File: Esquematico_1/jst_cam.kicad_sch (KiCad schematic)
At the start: 1 part, among them U5 AT7456E

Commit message: Update de algo nsq que puta
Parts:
- added J1, J2: Screw_Terminal_01x04, symbol Connector:Screw_Terminal_01x04
- added J3: Screw_Terminal_01x06, symbol Connector:Screw_Terminal_01x06
- added J4: Screw_Terminal_01x08, symbol Connector:Screw_Terminal_01x08
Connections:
- new net ELRS_UART_RX: J1.2 (Pin_2)
- new net ELRS_UART_TX: J1.1 (Pin_1)
- new net GND: J1.4 (Pin_4), J2.4 (Pin_4), J3.5 (Pin_5), J3.6 (Pin_6), J4.8 (Pin_8)
- new net V++: J3.4 (Pin_4)
- new net VIDEO_OSD_OUT: J3.3 (Pin_3)
- new net VTX_UART_RX: J3.2 (Pin_2)
- new net VTX_UART_TX: J3.1 (Pin_1)
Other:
- note added: "JST CAMARA"
- note added: "JST ELRS"
- note added: "JST ESC 4-1"
- note added: "JST VTX"
- moved on the sheet: U5

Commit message: Update
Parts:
- added C20: 10u, symbol Device:C
- added C21: 100n, symbol Device:C
- added FB2: FerriteBead, symbol Device:FerriteBead
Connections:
- net GND: now also C20.1, C21.1
- net MCO2: now reaches U5.5 (CLKIN)
- net 5v: now reaches J1.3 (Pin_3)
- net 5v: now also FB2.1
- new net 5vA: C20.2, C21.2, FB2.2
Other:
- moved on the sheet: J1, J2, J3, J4, U5

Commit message: Chau OSD
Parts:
- removed C20: 10u, symbol Device:C
- removed C21: 100n, symbol Device:C
- removed FB2: FerriteBead, symbol Device:FerriteBead
- removed U5: AT7456E, AT7456E:TSSOP-28_L9.7-W4.4-P0.65-LS6.4-BL-EP-2, symbol AT7456E:AT7456E
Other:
- note removed: "OSD"
- moved on the sheet: J1, J3, J4

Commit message: Correciones de tags
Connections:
- net VIDEO_OSD_OUT renamed VIDEO
- net VTX_UART_RX renamed RX_VTX
- net VTX_UART_TX renamed TX_VTX
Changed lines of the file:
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@@
 		)
 	)
-	(global_label "VTX_UART_TX"
+	(global_label "TX_VTX"
 		(shape input)
 		(at 119.38 35.56 180)
@@
 		)
 		(property "Intersheetrefs" "${INTERSHEET_REFS}"
-			(at 103.8841 35.56 0)
+			(at 109.5084 35.56 0)
 			(effects
 				(font
@@
 		)
 	)
-	(global_label "VIDEO_OSD_OUT"
+	(global_label "VIDEO"
 		(shape input)
 		(at 119.38 43.18 180)
@@
 		)
 		(property "Intersheetrefs" "${INTERSHEET_REFS}"
-			(at 101.1021 43.18 0)
+			(at 110.4759 43.18 0)
 			(effects
 				(font
@@
 		)
 	)
-	(global_label "VTX_UART_RX"
+	(global_label "RX_VTX"
 		(shape input)
 		(at 119.38 39.37 180)
@@
 		)
 		(property "Intersheetrefs" "${INTERSHEET_REFS}"
-			(at 103.5817 39.37 0)
+			(at 109.206 39.37 0)
 			(effects
 				(font
@@
 		)
 	)
-	(global_label "5v"
-		(shape input)
-		(at 186.69 48.26 180)
-		(fields_autoplaced yes)
-		(effects
-			(font
-				(size 1.27 1.27)
-				(thickness 0.254)
-				(bold yes)
-			)
-			(justify right)
-		)
-		(property "Intersheetrefs" "${INTERSHEET_REFS}"
-			(at 181.0517 48.26 0)
-			(effects
-				(font
-					(size 1.27 1.27)
-				)
-				(justify right)
-				(hide yes)
-			)
-		)
-	)
 	(symbol
 		(lib_id "power:GND")
@@
 					(unit 1)
 				)
+			)
+		)
+	)
+	(symbol
+		(lib_id "power:+3.3V")
+		(at 186.69 48.26 90)
+		(unit 1)
+		(exclude_from_sim no)
+		(in_bom yes)
+		(on_board yes)
+		(dnp no)
+		(fields_autoplaced yes)
+		(property "Reference" "#PWR027"
+			(at 190.5 48.26 0)
+			(effects
+				(font
+					(size 1.27 1.27)
+				)
+				(hide yes)
+			)
+		)
+		(property "Value" "5v"
+			(at 182.88 48.2599 90)
+			(effects
+				(font
+					(size 1.27 1.27)
+				)
+				(justify left)
+			)
+		)
+		(property "Footprint" ""
+			(at 186.69 48.26 0)
+			(effects
+				(font
+					(size 1.27 1.27)
+				)
+				(hide yes)
+			)
+		)
+		(property "Datasheet" ""
+			(at 186.69 48.26 0)
+			(effects
+				(font
+					(size 1.27 1.27)
+				)
+				(hide yes)
+			)
+		)
+		(property "Description" "Power symbol creates a global label with name \"+3.3V\""
+			(at 186.69 48.26 0)
+			(effects
+				(font
+					(size 1.27 1.27)
+				)
+				(hide yes)
+			)
+		)
+		(pin "1"
+		)
+		(instances
+			(project "Esquematico_1"
+				(path "/de2d80c1-c21c-478d-b724-17659b714c38/457e76de-adfe-4ec5-a818-c5970caa89a7"
+					(reference "#PWR027")
+					(unit 1)
+				)

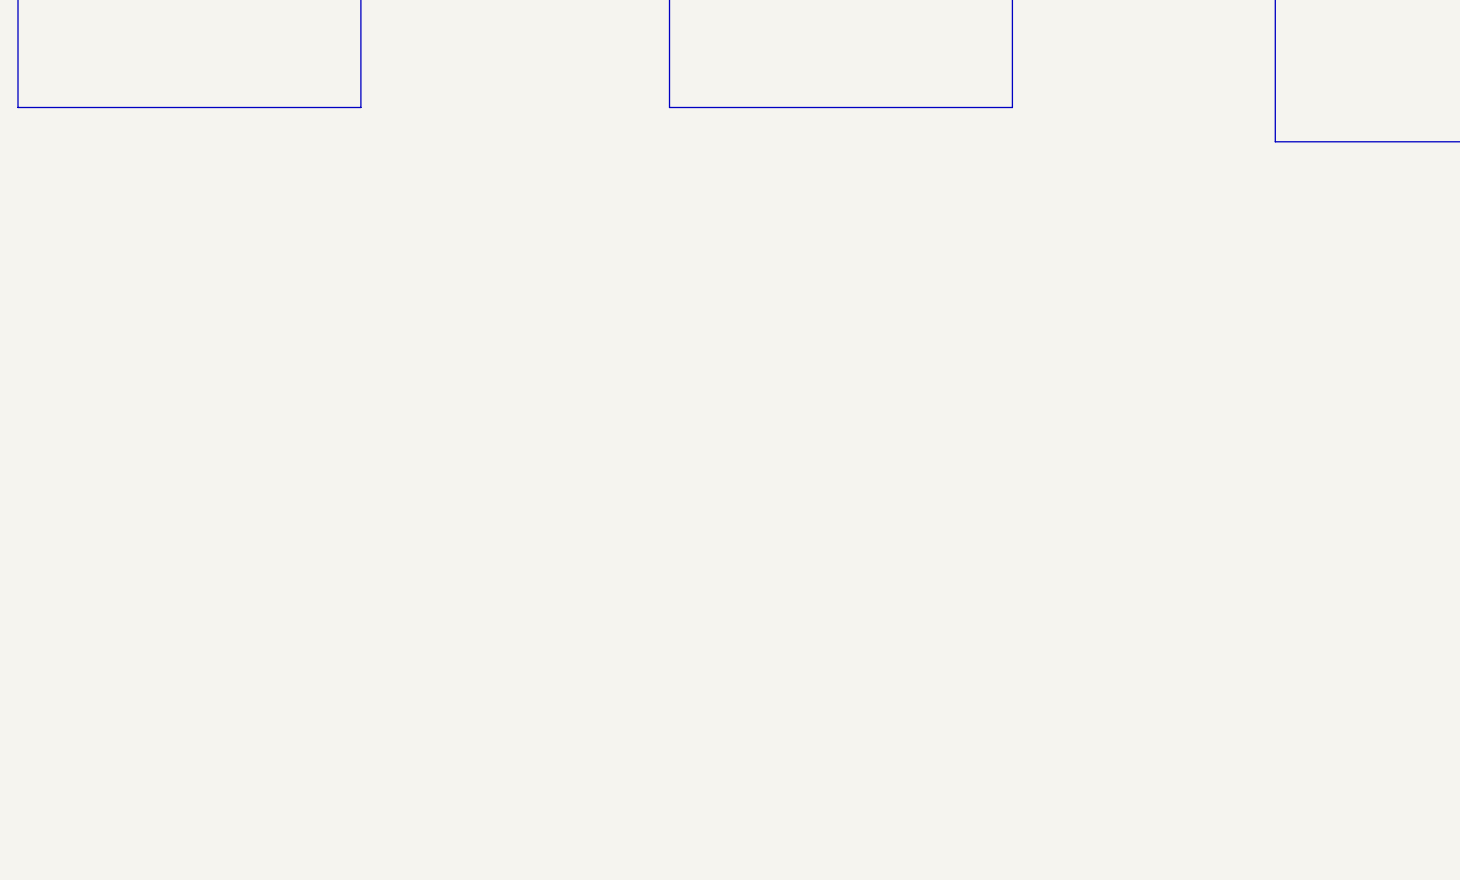
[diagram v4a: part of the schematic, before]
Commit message: UBS, botón de reset y boot, también por fin SWD
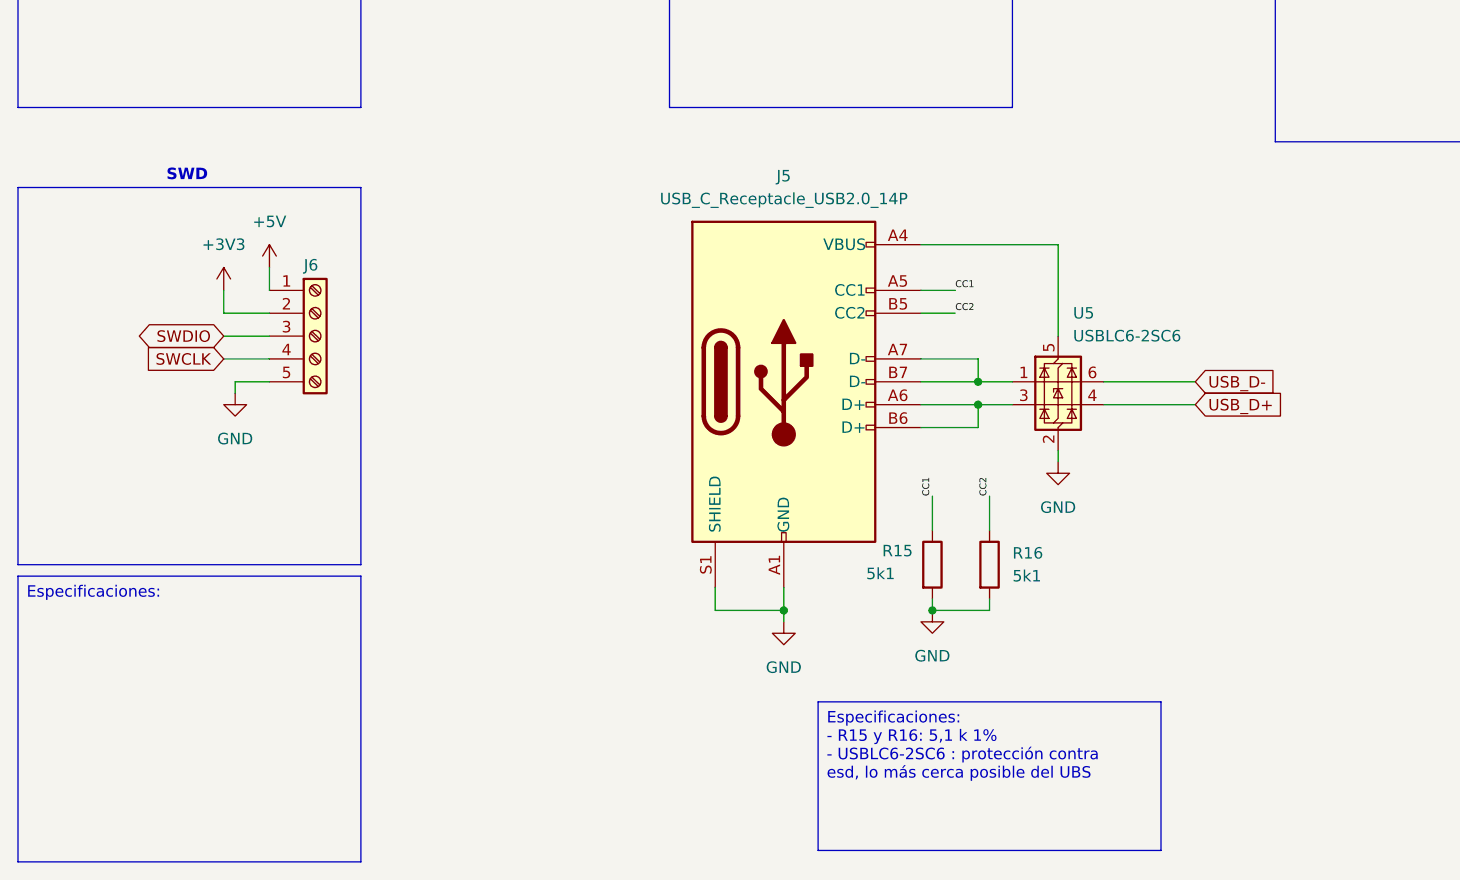
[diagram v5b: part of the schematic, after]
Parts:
- added J5: USB_C_Receptacle_USB2.0_14P, symbol Connector:USB_C_Receptacle_USB2.0_14P
- added J6: Screw_Terminal_01x05, symbol Connector:Screw_Terminal_01x05
- added R15, R16: 5k1, symbol Device:R
- added U5: USBLC6-2SC6, Package_TO_SOT_SMD:SOT-23-6, symbol Power_Protection:USBLC6-2SC6
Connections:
- net GND: now also J5.A1 (GND), J5.A12 (GND), J5.B1 (GND), J5.B12 (GND), J5.S1 (SHIELD), J6.5 (Pin_5), R15.2, R16.2, U5.2 (GND)
- new net: J5.A4 (VBUS), J5.A9 (VBUS), J5.B4 (VBUS), J5.B9 (VBUS), U5.5 (VBUS)
- new net: J5.A6 (D+), J5.B6 (D+), U5.3 (I/O2)
- new net: J5.A7 (D-), J5.B7 (D-), U5.1 (I/O1)
- new net +3V3: J6.2 (Pin_2)
- new net +5V: J6.1 (Pin_1)
- new net CC1: J5.A5 (CC1), R15.1
- new net CC2: J5.B5 (CC2), R16.1
- new net SWCLK: J6.4 (Pin_4)
- new net SWDIO: J6.3 (Pin_3)
- new net USB_D+: U5.4 (I/O2)
- new net USB_D-: U5.6 (I/O1)
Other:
- note added: "SWD"

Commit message: Descripciones
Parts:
- removed J2: Screw_Terminal_01x04, symbol Connector:Screw_Terminal_01x04
- added J2: Screw_Terminal_01x03, symbol Connector:Screw_Terminal_01x03
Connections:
- net V++ is gone; now on net 5v: J3.4 (Pin_4)
- net 5v: now also J2.1 (Pin_1)
- net GND: now also J2.2 (Pin_2)
- net VIDEO: now also J2.3 (Pin_3)
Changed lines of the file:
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@@
 		)
 	)
-	(text_box "Especificaciones: "
+	(text_box "Especificaciones: \nResolución de grabación de vídeo	720p\nFormato de captura de vídeo	MP4\nConsumo: 5V->150mAh\n		 12V->60mAh"
 		(exclude_from_sim no)
 		(at 237.49 66.04 0)
@@
 		)
 	)
-	(text_box "Especificaciones: "
+	(text_box "Especificaciones: \nTBS Unify Pro32 Nano 5G8 400mW\n"
 		(exclude_from_sim no)
 		(at 96.52 66.04 0)
@@
 		)
 	)
-	(text_box "Especificaciones: "
+	(text_box "Especificaciones: \nItem: BETAFPV SuperD ELRS 2.4GHz\nMCU: ESP32 PICO D4, dual SX1280(SX1281) (2.4GHz) \nTelemetry power: 20dBm (2.4GHz) \nWeight excluding antenna: 1.1g (2.4GHz)\nRF Frequency: 2.4GHz (ISM) \nInput voltage: +5V DC\nReceiver protocol: CRSF\nPCB size: 22mm x 14mm\n***Consumo???\n"
 		(exclude_from_sim no)
 		(at 163.83 66.04 0)
@@
 	(wire
 		(pts
-			(xy 264.16 48.26) (xy 267.97 48.26)
-		)
-		(stroke
-			(width 0)
-			(type default)
-		)
-	)
-	(wire
-		(pts
 			(xy 52.07 120.65) (xy 46.99 120.65)
 		)
@@
 	(wire
 		(pts
+			(xy 260.35 40.64) (xy 266.7 40.64)
+		)
+		(stroke
+			(width 0)
+			(type default)
+		)
+	)
+	(wire
+		(pts
 			(xy 127 50.8) (xy 127 54.61)
 		)
@@
 	(wire
 		(pts
-			(xy 264.16 49.53) (xy 264.16 48.26)
-		)
-		(stroke
-			(width 0)
-			(type default)
-		)
-	)
-	(wire
-		(pts
 			(xy 128.27 118.11) (xy 124.46 118.11)
 		)
@@
 		(pts
 			(xy 132.08 140.97) (xy 132.08 144.78)
+		)
+		(stroke
+			(width 0)
+			(type default)
+		)
+	)
+	(wire
+		(pts
+			(xy 261.62 45.72) (xy 266.7 45.72)
 		)
 		(stroke
@@
 				)
 				(justify left)
+				(hide yes)
+			)
+		)
+	)
+	(global_label "VIDEO"
+		(shape input)
+		(at 261.62 45.72 180)
+		(fields_autoplaced yes)
+		(effects
+			(font
+				(size 1.27 1.27)
+				(thickness 0.254)
+				(bold yes)
+			)
+			(justify right)
+		)
+		(property "Intersheetrefs" "${INTERSHEET_REFS}"
+			(at 252.7159 45.72 0)
+			(effects
+				(font
+					(size 1.27 1.27)
+				)
+				(justify right)
 				(hide yes)
 			)
@@
 		)
 	)
-	(global_label "V++"
-		(shape input)
-		(at 119.38 46.99 180)
-		(fields_autoplaced yes)
-		(effects
-			(font
-				(size 1.27 1.27)
-				(thickness 0.254)
-				(bold yes)
-			)
-			(justify right)
-		)
-		(property "Intersheetrefs" "${INTERSHEET_REFS}"
-			(at 111.6854 46.99 0)
-			(effects
-				(font
-					(size 1.27 1.27)
-				)
-				(justify right)
-				(hide yes)
-			)
-		)
-	)
 	(global_label "RX_VTX"
 		(shape input)
@@
 	)
 	(symbol
-		(lib_id "Connector:Screw_Terminal_01x04")
-		(at 273.05 43.18 0)
+		(lib_id "power:+3.3V")
+		(at 260.35 40.64 90)
 		(unit 1)
 		(exclude_from_sim no)
@@
 		(on_board yes)
 		(dnp no)
-		(property "Reference" "J2"
-			(at 271.78 37.846 0)
+		(fields_autoplaced yes)
+		(property "Reference" "#PWR045"
+			(at 264.16 40.64 0)
+			(effects
+				(font
+					(size 1.27 1.27)
+				)
+				(hide yes)
+			)
+		)
+		(property "Value" "5v"
+			(at 256.54 40.6399 90)
 			(effects
 				(font
@@
 			)
 		)
-		(property "Value" "Screw_Terminal_01x04"
-			(at 245.11 24.638 0)
-			(effects
-				(font
-					(size 1.27 1.27)
-				)
-				(justify left)
-			)
-		)
 		(property "Footprint" ""
-			(at 273.05 43.18 0)
-			(effects
-				(font
-					(size 1.27 1.27)
-				)
-				(hide yes)
-			)
-		)
-		(property "Datasheet" "~"
-			(at 273.05 43.18 0)
-			(effects
-				(font
-					(size 1.27 1.27)
-				)
-				(hide yes)
-			)
-		)
-		(property "Description" "Generic screw terminal, single row, 01x04, script generated (kicad-library-utils/schlib/autogen/connector/)"
-			(at 273.05 43.18 0)
-			(effects
-				(font
-					(size 1.27 1.27)
-				)
-				(hide yes)
-			)
-		)
-		(pin "3"
+			(at 260.35 40.64 0)
+			(effects
+				(font
+					(size 1.27 1.27)
+				)
+				(hide yes)
+			)
+		)
+		(property "Datasheet" ""
+			(at 260.35 40.64 0)
+			(effects
+				(font
+					(size 1.27 1.27)
+				)
+				(hide yes)
+			)
+		)
+		(property "Description" "Power symbol creates a global label with name \"+3.3V\""
+			(at 260.35 40.64 0)
+			(effects
+				(font
+					(size 1.27 1.27)
+				)
+				(hide yes)
+			)
 		)
 		(pin "1"
 		)
-		(pin "2"
-		)
-		(pin "4"
-		)
 		(instances
-			(project ""
+			(project "Esquematico_1"
 				(path "/de2d80c1-c21c-478d-b724-17659b714c38/457e76de-adfe-4ec5-a818-c5970caa89a7"
-					(reference "J2")
+					(reference "#PWR045")
 					(unit 1)
 				)
@@
 	)
 	(symbol
-		(lib_id "power:GND")
-		(at 264.16 49.53 0)
+		(lib_id "Connector:Screw_Terminal_01x03")
+		(at 271.78 43.18 0)
 		(unit 1)
 		(exclude_from_sim no)
@@
 		(on_board yes)
 		(dnp no)
-		(fields_autoplaced yes)
+		(property "Reference" "J2"
+			(at 270.256 37.592 0)
+			(effects
+				(font
+					(size 1.27 1.27)
+				)
+				(justify left)
+			)
+		)
+		(property "Value" "Screw_Terminal_01x03"
+			(at 245.364 24.384 0)
+			(effects
+				(font
+					(size 1.27 1.27)
+				)
+				(justify left)
+			)
+		)
+		(property "Footprint" ""
+			(at 271.78 43.18 0)
+			(effects
+				(font
+					(size 1.27 1.27)
+				)
+				(hide yes)
+			)
+		)
+		(property "Datasheet" "~"
+			(at 271.78 43.18 0)
+			(effects
+				(font
+					(size 1.27 1.27)
+				)
+				(hide yes)
+			)
+		)
+		(property "Description" "Generic screw terminal, single row, 01x03, script generated (kicad-library-utils/schlib/autogen/connector/)"
+			(at 271.78 43.18 0)
+			(effects
+				(font
+					(size 1.27 1.27)
+				)
+				(hide yes)
+			)
+		)
+		(pin "3"
+		)
+		(pin "1"
+		)
+		(pin "2"
+		)
+		(instances
+			(project ""
+				(path "/de2d80c1-c21c-478d-b724-17659b714c38/457e76de-adfe-4ec5-a818-c5970caa89a7"
+					(reference "J2")
+					(unit 1)
+				)
+			)
+		)
+	)
+	(symbol
+		(lib_id "power:GND")
+		(at 266.7 43.18 270)
+		(unit 1)
+		(exclude_from_sim no)
+		(in_bom yes)
+		(on_board yes)
+		(dnp no)
 		(property "Reference" "#PWR08"
-			(at 264.16 55.88 0)
+			(at 260.35 43.18 0)
 			(effects
 				(font
@@
 		)
 		(property "Value" "GND"
-			(at 264.16 54.61 0)
+			(at 261.62 43.18 90)
 			(effects
 				(font
@@
 		)
 		(property "Footprint" ""
-			(at 264.16 49.53 0)
+			(at 266.7 43.18 0)
 			(effects
 				(font
@@
 		)
 		(property "Datasheet" ""
-			(at 264.16 49.53 0)
+			(at 266.7 43.18 0)
 			(effects
 				(font
@@
 		)
 		(property "Description" "Power symbol creates a global label with name \"GND\" , ground"
-			(at 264.16 49.53 0)
+			(at 266.7 43.18 0)
 			(effects
 				(font
@@
 					(unit 1)
 				)
+			)
+		)
+	)
+	(symbol
+		(lib_id "power:+3.3V")
+		(at 119.38 46.99 90)
+		(unit 1)
+		(exclude_from_sim no)
+		(in_bom yes)
+		(on_board yes)
+		(dnp no)
+		(fields_autoplaced yes)
+		(property "Reference" "#PWR046"
+			(at 123.19 46.99 0)
+			(effects
+				(font
+					(size 1.27 1.27)
+				)
+				(hide yes)
+			)
+		)
+		(property "Value" "5v"
+			(at 115.57 46.9899 90)
+			(effects
+				(font
+					(size 1.27 1.27)
+				)
+				(justify left)
+			)
+		)
+		(property "Footprint" ""
+			(at 119.38 46.99 0)
+			(effects
+				(font
+					(size 1.27 1.27)
+				)
+				(hide yes)
+			)
+		)
+		(property "Datasheet" ""
+			(at 119.38 46.99 0)
+			(effects
+				(font
+					(size 1.27 1.27)
+				)
+				(hide yes)
+			)
+		)
+		(property "Description" "Power symbol creates a global label with name \"+3.3V\""
+			(at 119.38 46.99 0)
+			(effects
+				(font
+					(size 1.27 1.27)
+				)
+				(hide yes)
+			)
+		)
+		(pin "1"
+		)
+		(instances
+			(project "Esquematico_1"
+				(path "/de2d80c1-c21c-478d-b724-17659b714c38/457e76de-adfe-4ec5-a818-c5970caa89a7"
+					(reference "#PWR046")
+					(unit 1)
+				)

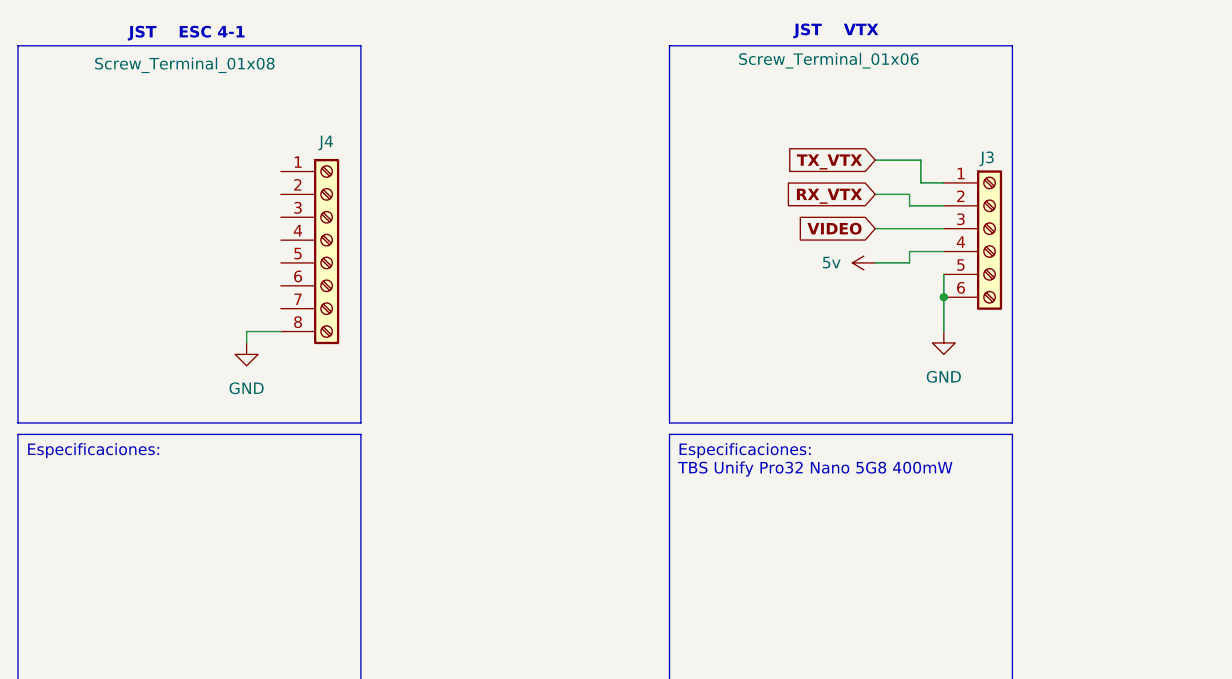
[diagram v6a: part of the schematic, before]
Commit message: Cambio de ESC
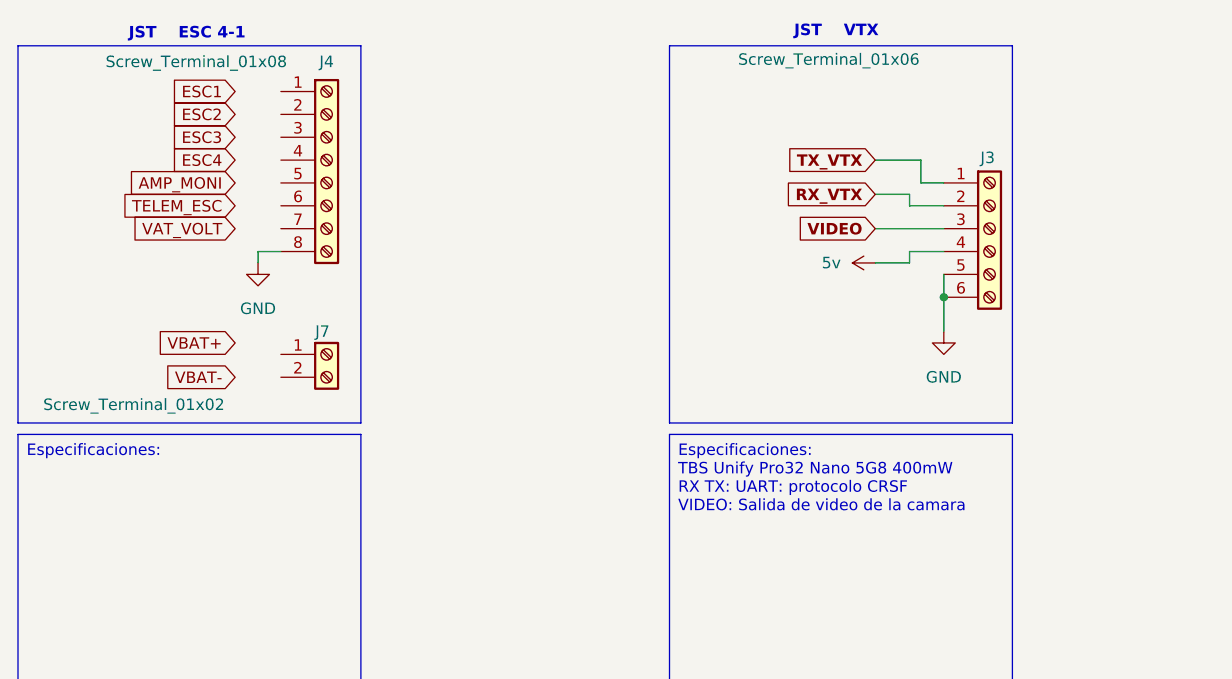
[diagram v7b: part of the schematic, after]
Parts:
- added J7: Screw_Terminal_01x02, symbol Connector:Screw_Terminal_01x02
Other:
- moved on the sheet: J4
